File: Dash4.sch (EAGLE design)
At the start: 9 parts

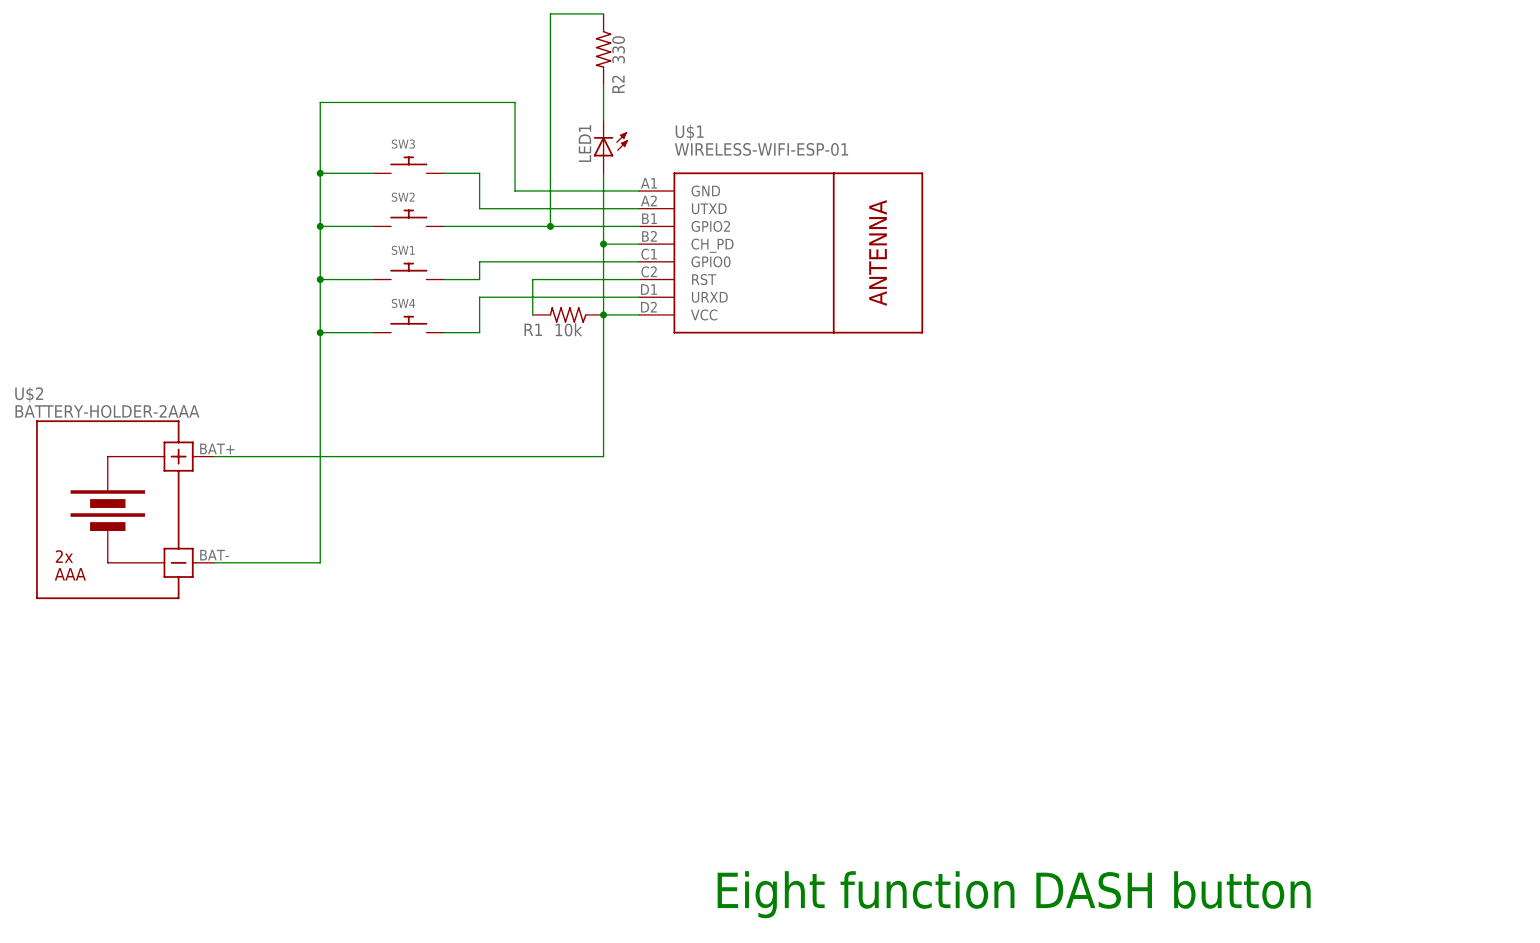
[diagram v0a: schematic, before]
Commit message: Added GPIO pinout drawing, cleaned up schematic
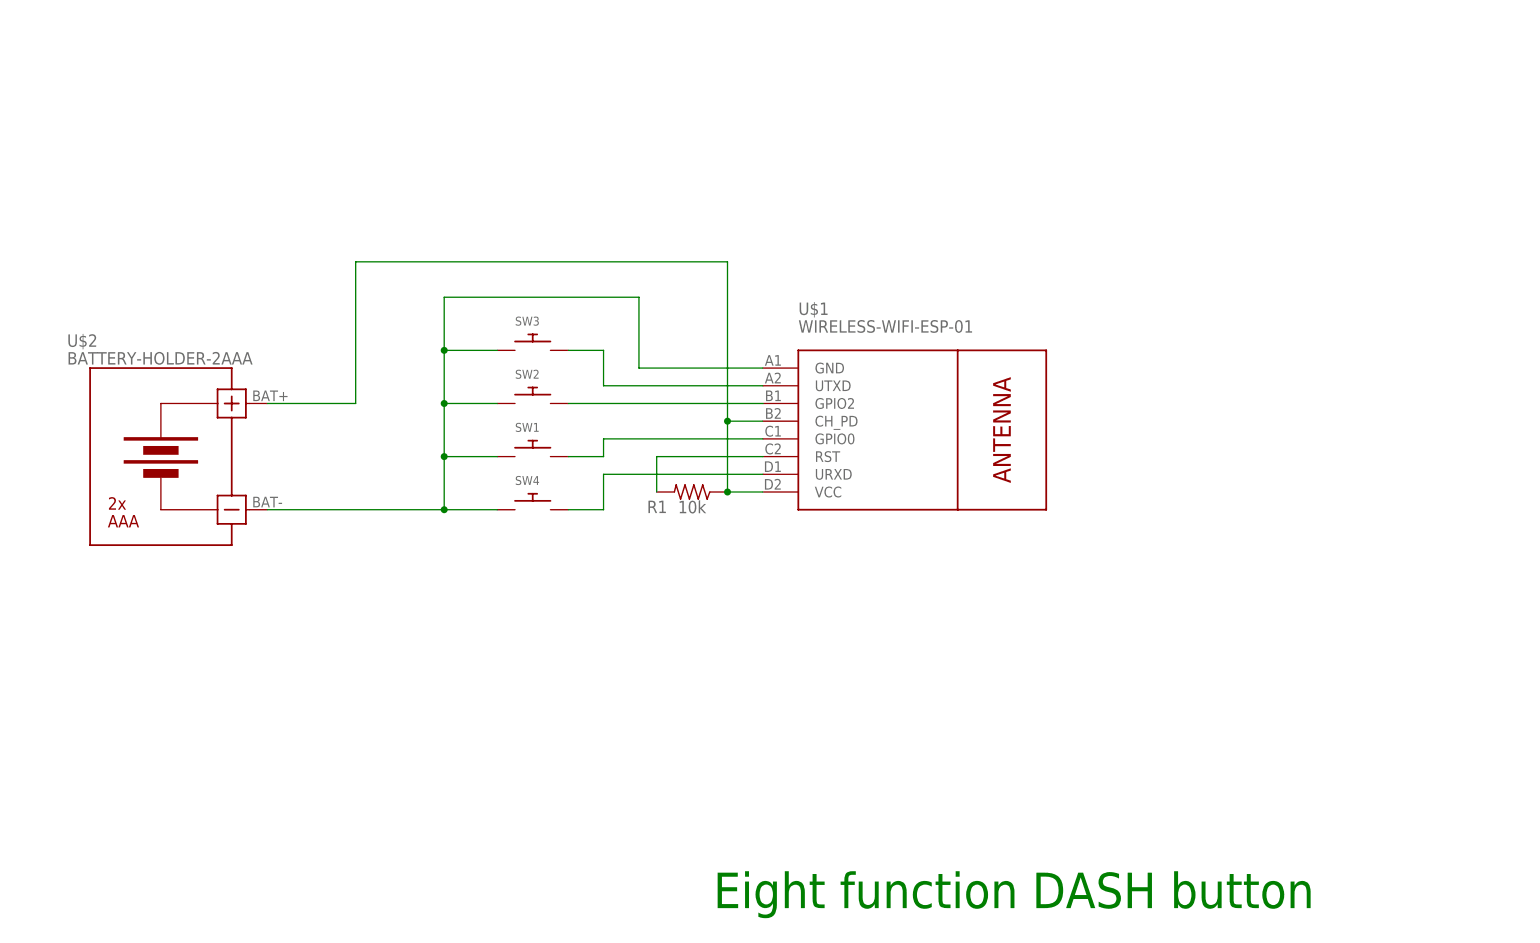
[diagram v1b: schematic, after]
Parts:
- removed LED1: (no value), adafruit:LED5MM
- removed R2: 330, adafruit:R-US_0207/9
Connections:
- removed net N$8: LED1.C, R2.2
- net N$2: no longer LED1.A
- net N$5: no longer R2.1
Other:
- moved on the sheet: R1, SW1, SW2, SW3, SW4, U$1, U$2
